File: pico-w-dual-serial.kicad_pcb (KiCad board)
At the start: 2 copper layers, 86.4 x 76.2 mm, 67 parts, among them J1 DB9_Male, J2 DB9_Male, J3 RAPC722X, SW1 Mode Button, U1 PicoW, U2 MAX3232, U3 LM7805_TO220

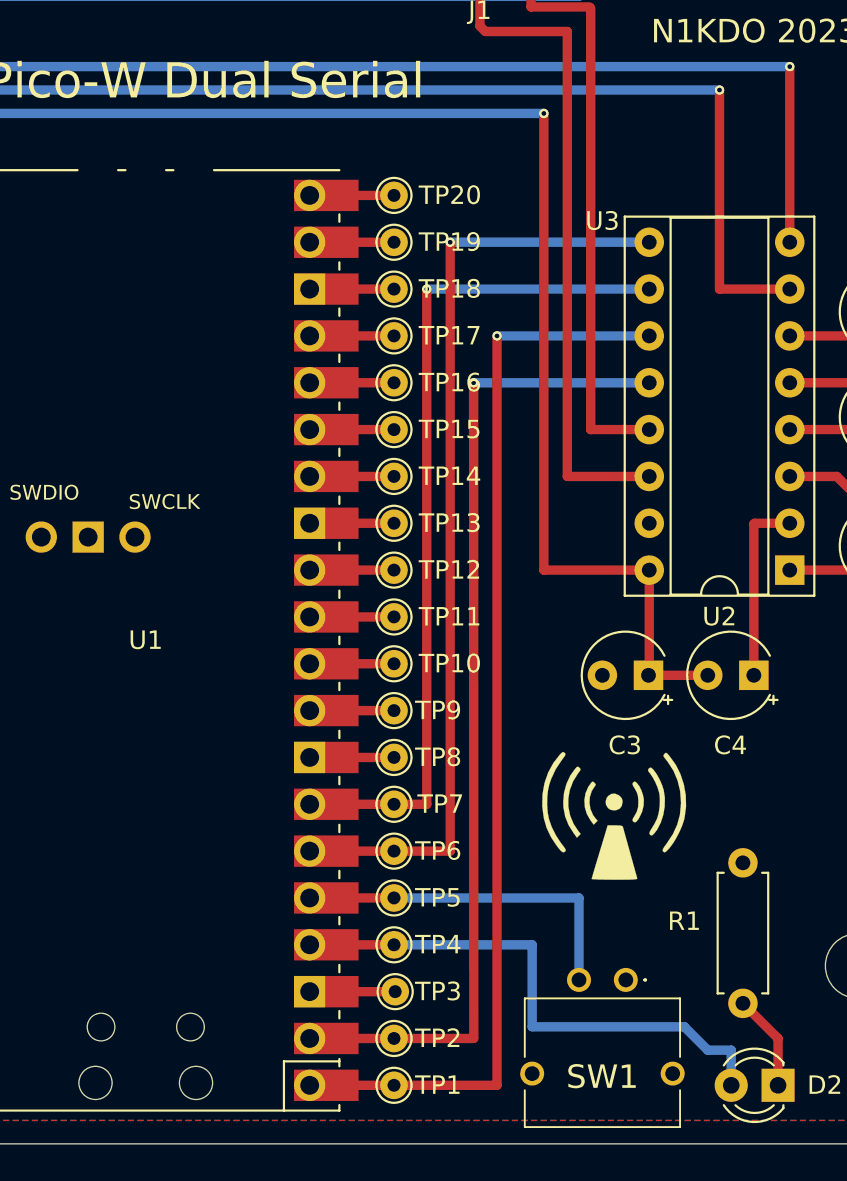
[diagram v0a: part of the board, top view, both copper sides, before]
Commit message: fix reversed TX2/RX2
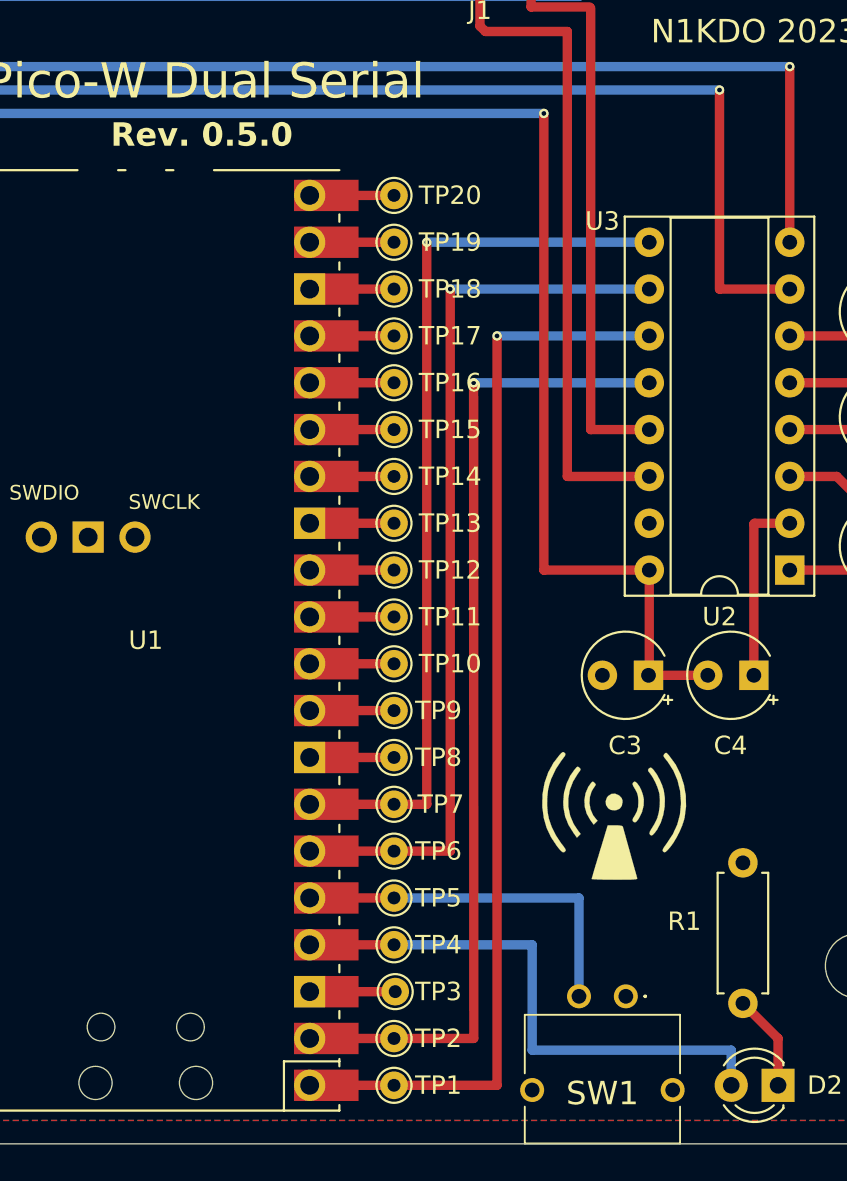
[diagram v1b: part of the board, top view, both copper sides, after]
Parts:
- moved SW1 0.89 mm to (92.7, 93.6)
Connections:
- TP6 pad 1: RX2 -> TX2
- TP7 pad 1: TX2 -> RX2
- U1 pad 6: RX2 -> TX2
- U1 pad 7: TX2 -> RX2
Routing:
- net TX2: track 46.3 -> 48.9 mm
- net RX2: track 51.4 -> 48.9 mm
- net Net-(D2-A): track 29.7 -> 30.5 mm
- net Net-(U1-GPIO3): track 19.0 -> 19.7 mm
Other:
- board text added: "Rev. 0.5.0"
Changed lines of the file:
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@@
   (title_block
     (title "Pico-W Dual Serial")
-    (date "2023-08-06")
-    (rev "0.4.0")
+    (date "2023-08-14")
+    (rev "0.5.0")
     (company "License CC-BY-SA https://creativecommons.org/licenses/by-sa/4.0/")
     (comment 1 "Drawn by N1KDO")
@@
       (stroke (width 0.05) (type solid)) (fill none) (layer "F.CrtYd"))
     (pad "1" thru_hole circle (at 0 0) (size 1.5 1.5) (drill 0.7) (layers "*.Cu" "*.Mask")
-      (net 33 "TX2") (pinfunction "1") (pintype "passive"))
+      (net 32 "RX2") (pinfunction "1") (pintype "passive"))
   )
   (footprint "TestPoint:TestPoint_THTPad_D1.5mm_Drill0.7mm" (layer "F.Cu")
@@
   )
   (footprint "parts:GB215AHB" (layer "F.Cu")
-    (at 92.71 92.71)
+    (at 92.71 93.599)
     (descr "GB215AH-B-3")
     (tags "Switch")
@@
       (net 31 "Net-(U1-GPIO3)") (pinfunction "GPIO3") (pintype "bidirectional"))
     (pad "6" thru_hole oval (at -8.89 -11.43 180) (size 1.7 1.7) (drill 1.02) (layers "*.Cu" "*.Mask")
-      (net 32 "RX2") (pinfunction "GPIO4") (pintype "bidirectional"))
+      (net 33 "TX2") (pinfunction "GPIO4") (pintype "bidirectional"))
     (pad "6" smd rect (at -8.89 -11.43 180) (size 3.5 1.7) (drill (offset -0.9 0)) (layers "F.Cu" "F.Mask")
-      (net 32 "RX2") (pinfunction "GPIO4") (pintype "bidirectional"))
+      (net 33 "TX2") (pinfunction "GPIO4") (pintype "bidirectional"))
     (pad "7" thru_hole oval (at -8.89 -8.89 180) (size 1.7 1.7) (drill 1.02) (layers "*.Cu" "*.Mask")
-      (net 33 "TX2") (pinfunction "GPIO5") (pintype "bidirectional"))
+      (net 32 "RX2") (pinfunction "GPIO5") (pintype "bidirectional"))
     (pad "7" smd rect (at -8.89 -8.89 180) (size 3.5 1.7) (drill (offset -0.9 0)) (layers "F.Cu" "F.Mask")
-      (net 33 "TX2") (pinfunction "GPIO5") (pintype "bidirectional"))
+      (net 32 "RX2") (pinfunction "GPIO5") (pintype "bidirectional"))
     (pad "8" thru_hole rect (at -8.89 -6.35 180) (size 1.7 1.7) (drill 1.02) (layers "*.Cu" "*.Mask")
       (net 4 "GND") (pinfunction "GND") (pintype "power_in") (thermal_bridge_angle 45))
@@
       (stroke (width 0.05) (type solid)) (fill none) (layer "F.CrtYd"))
     (pad "1" thru_hole circle (at 0 0 180) (size 1.5 1.5) (drill 0.7) (layers "*.Cu" "*.Mask")
-      (net 32 "RX2") (pinfunction "1") (pintype "passive"))
+      (net 33 "TX2") (pinfunction "1") (pintype "passive"))
   )
   (footprint "TestPoint:TestPoint_THTPad_D1.5mm_Drill0.7mm" (layer "F.Cu")
@@
     (effects (font (size 1.905 1.905) (thickness 0.254)) (justify bottom))
   )
+  (gr_text "Rev. 0.5.0" (at 64.77 47.625) (layer "F.SilkS")
+    (effects (font (size 1.27 1.27) (thickness 0.3) bold) (justify left bottom))
+  )
   (gr_text "N1KDO 2023" (at 99.695 41.275) (layer "F.SilkS")
     (effects (font (size 1.27 1.27) (thickness 0.254)))
@@
   (segment (start 75.565 90.805) (end 80.137 90.805) (width 0.508) (layer "F.Cu") (net 13))
   (segment (start 98.425 96.52) (end 98.425 98.425) (width 0.508) (layer "B.Cu") (net 13))
-  (segment (start 87.63 95.25) (end 95.885 95.25) (width 0.508) (layer "B.Cu") (net 13))
-  (segment (start 95.885 95.25) (end 97.155 96.52) (width 0.508) (layer "B.Cu") (net 13))
-  (segment (start 87.63 90.805) (end 87.63 95.25) (width 0.508) (layer "B.Cu") (net 13))
-  (segment (start 97.155 96.52) (end 98.425 96.52) (width 0.508) (layer "B.Cu") (net 13))
+  (segment (start 87.63 90.805) (end 87.63 96.52) (width 0.508) (layer "B.Cu") (net 13))
+  (segment (start 98.425 96.52) (end 87.63 96.52) (width 0.508) (layer "B.Cu") (net 13))
   (segment (start 80.137 90.805) (end 87.63 90.805) (width 0.508) (layer "B.Cu") (net 13))
   (segment (start 85.725 98.425) (end 85.725 57.785) (width 0.508) (layer "F.Cu") (net 19))
@@
   (segment (start 75.565 88.265) (end 80.137 88.265) (width 0.508) (layer "F.Cu") (net 31))
   (segment (start 80.137 88.265) (end 90.17 88.265) (width 0.508) (layer "B.Cu") (net 31))
-  (segment (start 90.17 88.265) (end 90.17 92.71) (width 0.508) (layer "B.Cu") (net 31))
-  (segment (start 75.565 85.725) (end 80.137 85.725) (width 0.508) (layer "F.Cu") (net 32))
-  (segment (start 80.137 85.725) (end 83.185 85.725) (width 0.508) (layer "F.Cu") (net 32))
-  (segment (start 83.185 85.725) (end 83.185 52.705) (width 0.508) (layer "F.Cu") (net 32))
-  (via (at 83.185 52.705) (size 0.508) (drill 0.254) (layers "F.Cu" "B.Cu") (net 32))
-  (segment (start 93.98 52.705) (end 83.185 52.705) (width 0.508) (layer "B.Cu") (net 32))
-  (segment (start 81.915 83.185) (end 81.915 55.245) (width 0.508) (layer "F.Cu") (net 33))
-  (segment (start 80.137 83.185) (end 81.915 83.185) (width 0.508) (layer "F.Cu") (net 33))
-  (segment (start 80.137 83.185) (end 75.565 83.185) (width 0.508) (layer "F.Cu") (net 33))
-  (via (at 81.915 55.245) (size 0.508) (drill 0.254) (layers "F.Cu" "B.Cu") (net 33))
-  (segment (start 93.98 55.245) (end 81.925 55.245) (width 0.508) (layer "B.Cu") (net 33))
+  (segment (start 90.17 88.265) (end 90.17 93.345) (width 0.508) (layer "B.Cu") (net 31))
+  (segment (start 81.915 52.705) (end 81.915 83.185) (width 0.508) (layer "F.Cu") (net 32))
+  (segment (start 80.137 83.185) (end 81.915 83.185) (width 0.508) (layer "F.Cu") (net 32))
+  (segment (start 80.137 83.185) (end 75.565 83.185) (width 0.508) (layer "F.Cu") (net 32))
+  (via (at 81.915 52.705) (size 0.508) (drill 0.254) (layers "F.Cu" "B.Cu") (net 32))
+  (segment (start 93.98 52.705) (end 81.915 52.705) (width 0.508) (layer "B.Cu") (net 32))
+  (segment (start 75.565 85.725) (end 80.137 85.725) (width 0.508) (layer "F.Cu") (net 33))
+  (segment (start 80.137 85.725) (end 83.185 85.725) (width 0.508) (layer "F.Cu") (net 33))
+  (segment (start 83.185 55.245) (end 83.185 85.725) (width 0.508) (layer "F.Cu") (net 33))
+  (via (at 83.185 55.245) (size 0.508) (drill 0.254) (layers "F.Cu" "B.Cu") (net 33))
+  (segment (start 93.98 55.245) (end 83.185 55.245) (width 0.508) (layer "B.Cu") (net 33))
   (segment (start 80.137 78.105) (end 78.105 78.105) (width 0.508) (layer "F.Cu") (net 34))
   (segment (start 75.565 75.565) (end 80.137 75.565) (width 0.508) (layer "F.Cu") (net 35))

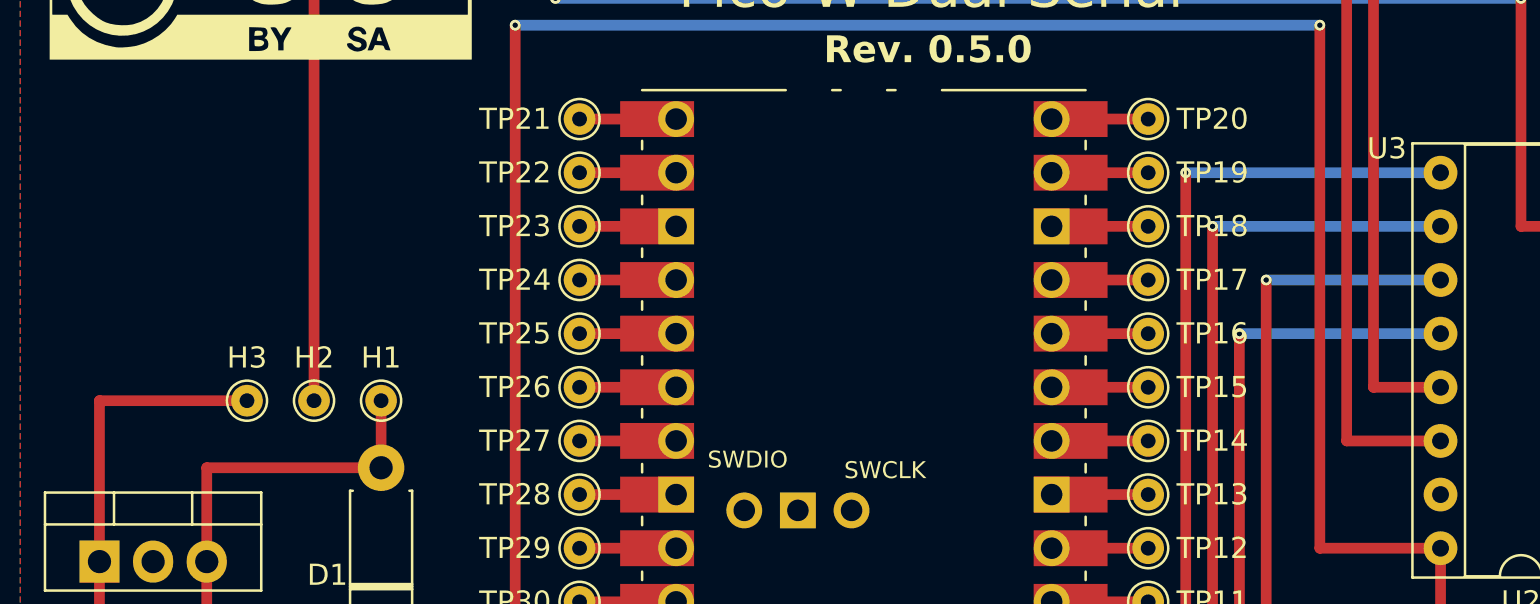
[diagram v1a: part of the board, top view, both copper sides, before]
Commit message: new pic, better BOM
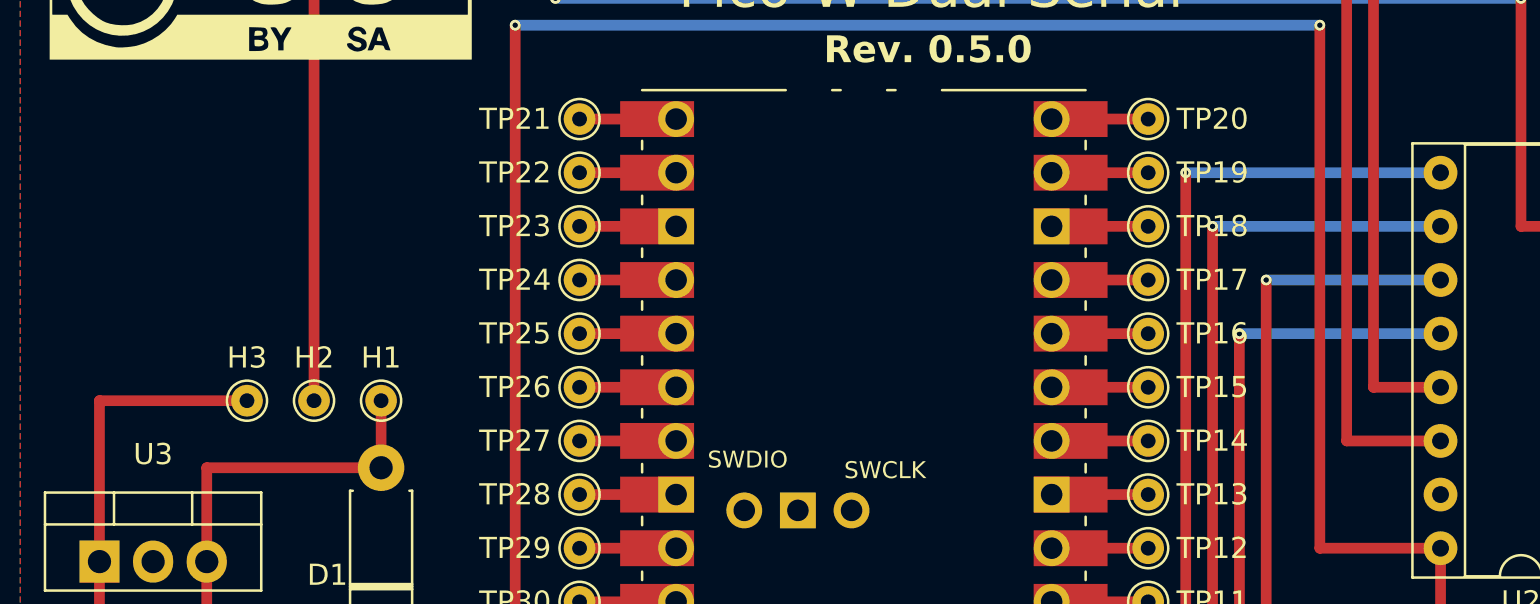
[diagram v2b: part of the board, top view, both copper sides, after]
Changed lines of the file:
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@@
     (property "ki_keywords" "Voltage Regulator 1A Positive")
     (attr through_hole)
-    (fp_text reference "U3" (at 60.96 -19.558 180) (layer "F.SilkS")
+    (fp_text reference "U3" (at 2.54 -5.08 180) (layer "F.SilkS")
         (effects (font (size 1 1) (thickness 0.15)))
     )
